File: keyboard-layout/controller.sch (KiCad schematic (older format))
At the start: 15 parts, among them J1 USB_mini_micro_B, SW1 SW_PUSH, X1 XTAL_GND

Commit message: mx footprints
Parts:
- removed C1, C2: 22p, Capacitors_SMD:C_0805_HandSoldering, symbol C
- removed C3, C4, C5: 0.1u, Capacitors_SMD:C_0805_HandSoldering, symbol C
- removed C6: 4.7u, Capacitors_SMD:C_0805_HandSoldering, symbol C
- removed C7: 1u, Capacitors_SMD:C_0805_HandSoldering, symbol C
- removed J1: USB_mini_micro_B, keyboard_parts:USB_miniB_hirose_5S8, symbol USB_mini_micro_B
- removed MCU1: AT90USB1286, AT90USB1286-AU:QFP80P1600X1600X120-64N, symbol AT90USB1286
- removed R1, R2: 10k, Resistors_SMD:R_0805_HandSoldering, symbol R
- removed R3, R4: 22, Resistors_SMD:R_0805_HandSoldering, symbol R
- removed SW1: SW_PUSH, Buttons_Switches_SMD:SW_SPST_TL3342, symbol SW_PUSH
- removed X1: XTAL_GND, Crystals:Crystal_SMD_SeikoEpson_FA238-4pin_3.2x2.5mm, symbol XTAL_GND
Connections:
- no-connect marks 45 -> 0
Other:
- note removed: "HWB (Bootloader)"

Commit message: pcb progress
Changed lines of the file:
@@
 $EndDescr
 $Sheet
-S 8100 2050 2100 1650
+S 5000 1400 1400 3000
 U 5AFAEA09
 F0 "Keyboard Matrix" 60
 F1 "Matrix.sch" 60
-F2 "col0" I L 8100 3000 60
-F3 "col1" I L 8100 3150 60
-F4 "row0" I L 8100 2700 60
-F5 "row1" I L 8100 2850 60
+F2 "row0" I L 5000 1500 60
+F3 "row1" I L 5000 1600 60
+F4 "col0" I L 5000 2100 60
+F5 "row2" I L 5000 1700 60
+F6 "row3" I L 5000 1800 60
+F7 "row4" I L 5000 1900 60
+F8 "row5" I L 5000 2000 60
+F9 "col1" I L 5000 2200 60
+F10 "col2" I L 5000 2300 60
+F11 "col3" I L 5000 2400 60
+F12 "col4" I L 5000 2500 60
+F13 "col5" I L 5000 2600 60
+F14 "col6" I L 5000 2700 60
+F15 "col7" I L 5000 2800 60
+F16 "col8" I L 5000 2900 60
+F17 "col9" I L 5000 3000 60
+F18 "col10" I L 5000 3100 60
+F19 "col11" I L 5000 3200 60
+F20 "col12" I L 5000 3300 60
+F21 "col13" I L 5000 3400 60
+F22 "col14" I L 5000 3500 60
+F23 "col15" I L 5000 3600 60
+F24 "col16" I L 5000 3700 60
+F25 "col17" I L 5000 3800 60
+F26 "col18" I L 5000 3900 60
+F27 "col19" I L 5000 4000 60
+F28 "col20" I L 5000 4100 60
 $EndSheet
+Wire Wire Line
+	3250 1500 5000 1500
+Wire Wire Line
+	5000 1600 3250 1600
 $Sheet
-S 4950 2050 1400 1650
+S 1850 1400 1400 3000
 U 5B003DFC
 F0 "MCU" 60
 F1 "MCU.sch" 60
-F2 "row0" I R 6350 2700 60
-F3 "row1" I R 6350 2850 60
-F4 "col0" I R 6350 3000 60
-F5 "col1" I R 6350 3150 60
+F2 "row0" I R 3250 1500 60
+F3 "row1" I R 3250 1600 60
+F4 "row2" I R 3250 1700 60
+F5 "row3" I R 3250 1800 60
+F6 "row4" I R 3250 1900 60
+F7 "row5" I R 3250 2000 60
+F8 "col0" I R 3250 2100 60
+F9 "col1" I R 3250 2200 60
+F10 "col2" I R 3250 2300 60
+F11 "col3" I R 3250 2400 60
+F12 "col4" I R 3250 2500 60
+F13 "col5" I R 3250 2600 60
+F14 "col6" I R 3250 2700 60
+F15 "col7" I R 3250 2800 60
+F16 "col8" I R 3250 2900 60
+F17 "col9" I R 3250 3000 60
+F18 "col10" I R 3250 3100 60
+F19 "col11" I R 3250 3200 60
+F20 "col12" I R 3250 3300 60
+F21 "col13" I R 3250 3400 60
+F22 "col14" I R 3250 3500 60
+F23 "col15" I R 3250 3600 60
+F24 "col16" I R 3250 3700 60
+F25 "col17" I R 3250 3800 60
+F26 "col18" I R 3250 3900 60
+F27 "col19" I R 3250 4000 60
+F28 "col20" I R 3250 4100 60
 $EndSheet
 Wire Wire Line
-	6350 2700 8100 2700
+	3250 1700 5000 1700
 Wire Wire Line
-	6350 2850 8100 2850
+	5000 1700 5000 1800
 Wire Wire Line
-	6350 3000 8100 3000
+	5000 1800 3250 1800
 Wire Wire Line
-	8100 3150 6350 3150
+	3250 1900 5000 1900
+Wire Wire Line
+	5000 2000 3250 2000
+Wire Wire Line
+	3250 2100 5000 2100
+Wire Wire Line
+	5000 2200 3250 2200
+Wire Wire Line
+	3250 2300 5000 2300
+Wire Wire Line
+	5000 2400 3250 2400
+Wire Wire Line
+	3250 2500 5000 2500
+Wire Wire Line
+	5000 2600 3250 2600
+Wire Wire Line
+	3250 2700 5000 2700
+Wire Wire Line
+	5000 2800 3250 2800
+Wire Wire Line
+	3250 2900 5000 2900
+Wire Wire Line
+	5000 3000 3250 3000
+Wire Wire Line
+	3250 3100 5000 3100
+Wire Wire Line
+	5000 3200 3250 3200
+Wire Wire Line
+	3250 3300 5000 3300
+Wire Wire Line
+	5000 3400 3250 3400
+Wire Wire Line
+	3250 3500 5000 3500
+Wire Wire Line
+	5000 3600 3250 3600
+Wire Wire Line
+	3250 3700 5000 3700
+Wire Wire Line
+	5000 3800 3250 3800
+Wire Wire Line
+	3250 3900 5000 3900
+Wire Wire Line
+	5000 4000 3250 4000
+Wire Wire Line
+	3250 4100 5000 4100
 $EndSCHEMATC

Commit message: python scripting
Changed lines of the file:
@@
 F6 "row3" I L 5000 1800 60
 F7 "row4" I L 5000 1900 60
-F8 "row5" I L 5000 2000 60
-F9 "col1" I L 5000 2200 60
-F10 "col2" I L 5000 2300 60
-F11 "col3" I L 5000 2400 60
-F12 "col4" I L 5000 2500 60
-F13 "col5" I L 5000 2600 60
-F14 "col6" I L 5000 2700 60
-F15 "col7" I L 5000 2800 60
-F16 "col8" I L 5000 2900 60
-F17 "col9" I L 5000 3000 60
-F18 "col10" I L 5000 3100 60
-F19 "col11" I L 5000 3200 60
-F20 "col12" I L 5000 3300 60
-F21 "col13" I L 5000 3400 60
-F22 "col14" I L 5000 3500 60
-F23 "col15" I L 5000 3600 60
-F24 "col16" I L 5000 3700 60
-F25 "col17" I L 5000 3800 60
-F26 "col18" I L 5000 3900 60
-F27 "col19" I L 5000 4000 60
-F28 "col20" I L 5000 4100 60
+F8 "col1" I L 5000 2200 60
+F9 "col2" I L 5000 2300 60
+F10 "col3" I L 5000 2400 60
+F11 "col4" I L 5000 2500 60
+F12 "col5" I L 5000 2600 60
+F13 "col6" I L 5000 2700 60
+F14 "col7" I L 5000 2800 60
+F15 "col8" I L 5000 2900 60
+F16 "col9" I L 5000 3000 60
+F17 "col10" I L 5000 3100 60
+F18 "col11" I L 5000 3200 60
+F19 "col12" I L 5000 3300 60
+F20 "col13" I L 5000 3400 60
+F21 "col14" I L 5000 3500 60
+F22 "col15" I L 5000 3600 60
+F23 "col16" I L 5000 3700 60
+F24 "col17" I L 5000 3800 60
+F25 "col18" I L 5000 3900 60
+F26 "col19" I L 5000 4000 60
+F27 "col20" I L 5000 4100 60
 $EndSheet
 Wire Wire Line
@@
 F5 "row3" I R 3250 1800 60
 F6 "row4" I R 3250 1900 60
-F7 "row5" I R 3250 2000 60
-F8 "col0" I R 3250 2100 60
-F9 "col1" I R 3250 2200 60
-F10 "col2" I R 3250 2300 60
-F11 "col3" I R 3250 2400 60
-F12 "col4" I R 3250 2500 60
-F13 "col5" I R 3250 2600 60
-F14 "col6" I R 3250 2700 60
-F15 "col7" I R 3250 2800 60
-F16 "col8" I R 3250 2900 60
-F17 "col9" I R 3250 3000 60
-F18 "col10" I R 3250 3100 60
-F19 "col11" I R 3250 3200 60
-F20 "col12" I R 3250 3300 60
-F21 "col13" I R 3250 3400 60
-F22 "col14" I R 3250 3500 60
-F23 "col15" I R 3250 3600 60
-F24 "col16" I R 3250 3700 60
-F25 "col17" I R 3250 3800 60
-F26 "col18" I R 3250 3900 60
-F27 "col19" I R 3250 4000 60
-F28 "col20" I R 3250 4100 60
+F7 "col0" I R 3250 2100 60
+F8 "col1" I R 3250 2200 60
+F9 "col2" I R 3250 2300 60
+F10 "col3" I R 3250 2400 60
+F11 "col4" I R 3250 2500 60
+F12 "col5" I R 3250 2600 60
+F13 "col6" I R 3250 2700 60
+F14 "col7" I R 3250 2800 60
+F15 "col8" I R 3250 2900 60
+F16 "col9" I R 3250 3000 60
+F17 "col10" I R 3250 3100 60
+F18 "col11" I R 3250 3200 60
+F19 "col12" I R 3250 3300 60
+F20 "col13" I R 3250 3400 60
+F21 "col14" I R 3250 3500 60
+F22 "col15" I R 3250 3600 60
+F23 "col16" I R 3250 3700 60
+F24 "col17" I R 3250 3800 60
+F25 "col18" I R 3250 3900 60
+F26 "col19" I R 3250 4000 60
+F27 "col20" I R 3250 4100 60
 $EndSheet
 Wire Wire Line
@@
 	3250 1900 5000 1900
 Wire Wire Line
-	5000 2000 3250 2000
-Wire Wire Line
 	3250 2100 5000 2100

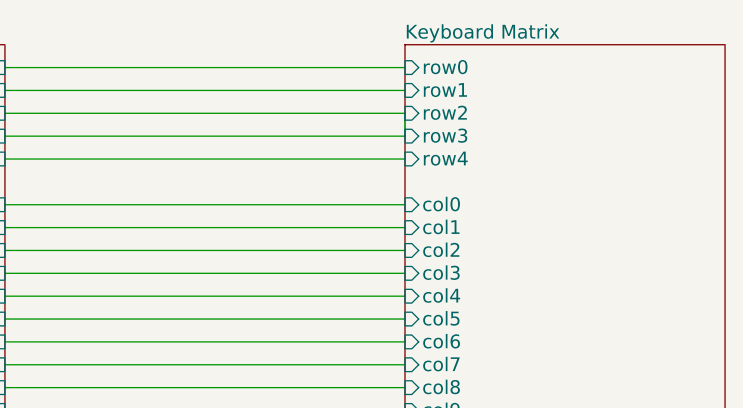
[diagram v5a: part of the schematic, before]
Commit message: pcb without leds finished
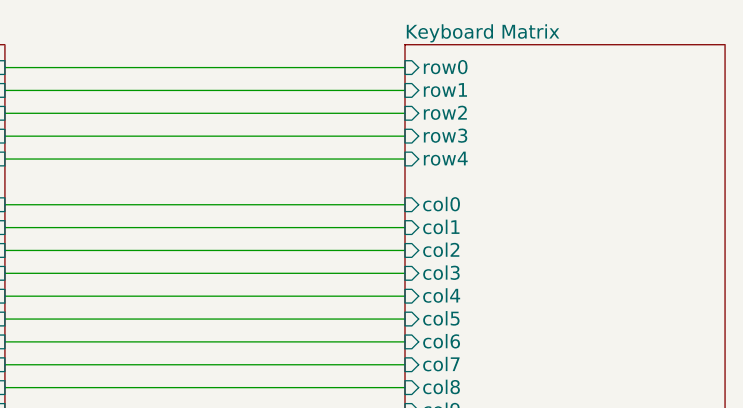
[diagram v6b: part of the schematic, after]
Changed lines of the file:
@@
 Comment4 ""
 $EndDescr
-$Sheet
-S 5000 1400 1400 3000
-U 5AFAEA09
-F0 "Keyboard Matrix" 60
-F1 "Matrix.sch" 60
-F2 "row0" I L 5000 1500 60
-F3 "row1" I L 5000 1600 60
-F4 "col0" I L 5000 2100 60
-F5 "row2" I L 5000 1700 60
-F6 "row3" I L 5000 1800 60
-F7 "row4" I L 5000 1900 60
-F8 "col1" I L 5000 2200 60
-F9 "col2" I L 5000 2300 60
-F10 "col3" I L 5000 2400 60
-F11 "col4" I L 5000 2500 60
-F12 "col5" I L 5000 2600 60
-F13 "col6" I L 5000 2700 60
-F14 "col7" I L 5000 2800 60
-F15 "col8" I L 5000 2900 60
-F16 "col9" I L 5000 3000 60
-F17 "col10" I L 5000 3100 60
-F18 "col11" I L 5000 3200 60
-F19 "col12" I L 5000 3300 60
-F20 "col13" I L 5000 3400 60
-F21 "col14" I L 5000 3500 60
-F22 "col15" I L 5000 3600 60
-F23 "col16" I L 5000 3700 60
-F24 "col17" I L 5000 3800 60
-F25 "col18" I L 5000 3900 60
-F26 "col19" I L 5000 4000 60
-F27 "col20" I L 5000 4100 60
-$EndSheet
 Wire Wire Line
 	3250 1500 5000 1500
@@
 F27 "col20" I R 3250 4100 60
 $EndSheet
-Wire Wire Line
-	3250 1700 5000 1700
-Wire Wire Line
-	5000 1700 5000 1800
-Wire Wire Line
-	5000 1800 3250 1800
-Wire Wire Line
-	3250 1900 5000 1900
 Wire Wire Line
 	3250 2100 5000 2100
@@
 Wire Wire Line
 	3250 4100 5000 4100
+$Sheet
+S 5000 1400 1400 3000
+U 5AFAEA09
+F0 "Keyboard Matrix" 60
+F1 "Matrix.sch" 60
+F2 "row0" I L 5000 1500 60
+F3 "row1" I L 5000 1600 60
+F4 "col0" I L 5000 2100 60
+F5 "row2" I L 5000 1700 60
+F6 "row3" I L 5000 1800 60
+F7 "row4" I L 5000 1900 60
+F8 "col1" I L 5000 2200 60
+F9 "col2" I L 5000 2300 60
+F10 "col3" I L 5000 2400 60
+F11 "col4" I L 5000 2500 60
+F12 "col5" I L 5000 2600 60
+F13 "col6" I L 5000 2700 60
+F14 "col7" I L 5000 2800 60
+F15 "col8" I L 5000 2900 60
+F16 "col9" I L 5000 3000 60
+F17 "col10" I L 5000 3100 60
+F18 "col11" I L 5000 3200 60
+F19 "col12" I L 5000 3300 60
+F20 "col13" I L 5000 3400 60
+F21 "col14" I L 5000 3500 60
+F22 "col15" I L 5000 3600 60
+F23 "col16" I L 5000 3700 60
+F24 "col17" I L 5000 3800 60
+F25 "col18" I L 5000 3900 60
+F26 "col19" I L 5000 4000 60
+F27 "col20" I L 5000 4100 60
+$EndSheet
+Wire Wire Line
+	3250 1900 5000 1900
+Wire Wire Line
+	5000 1800 3250 1800
+Wire Wire Line
+	3250 1700 5000 1700
 $EndSCHEMATC

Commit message: Leds
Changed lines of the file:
@@
 $Descr A4 11693 8268
 encoding utf-8
-Sheet 1 3
+Sheet 1 4
 Title ""
 Date ""
@@
 $EndDescr
 Wire Wire Line
-	3250 1500 5000 1500
+	5600 1650 7350 1650
 Wire Wire Line
-	5000 1600 3250 1600
+	7350 1750 5600 1750
 $Sheet
-S 1850 1400 1400 3000
+S 4200 1550 1400 3000
 U 5B003DFC
 F0 "MCU" 60
 F1 "MCU.sch" 60
-F2 "row0" I R 3250 1500 60
-F3 "row1" I R 3250 1600 60
-F4 "row2" I R 3250 1700 60
-F5 "row3" I R 3250 1800 60
-F6 "row4" I R 3250 1900 60
-F7 "col0" I R 3250 2100 60
-F8 "col1" I R 3250 2200 60
-F9 "col2" I R 3250 2300 60
-F10 "col3" I R 3250 2400 60
-F11 "col4" I R 3250 2500 60
-F12 "col5" I R 3250 2600 60
-F13 "col6" I R 3250 2700 60
-F14 "col7" I R 3250 2800 60
-F15 "col8" I R 3250 2900 60
-F16 "col9" I R 3250 3000 60
-F17 "col10" I R 3250 3100 60
-F18 "col11" I R 3250 3200 60
-F19 "col12" I R 3250 3300 60
-F20 "col13" I R 3250 3400 60
-F21 "col14" I R 3250 3500 60
-F22 "col15" I R 3250 3600 60
-F23 "col16" I R 3250 3700 60
-F24 "col17" I R 3250 3800 60
-F25 "col18" I R 3250 3900 60
-F26 "col19" I R 3250 4000 60
-F27 "col20" I R 3250 4100 60
+F2 "row0" I R 5600 1650 60
+F3 "row1" I R 5600 1750 60
+F4 "row2" I R 5600 1850 60
+F5 "row3" I R 5600 1950 60
+F6 "row4" I R 5600 2050 60
+F7 "col0" I R 5600 2250 60
+F8 "col1" I R 5600 2350 60
+F9 "col2" I R 5600 2450 60
+F10 "col3" I R 5600 2550 60
+F11 "col4" I R 5600 2650 60
+F12 "col5" I R 5600 2750 60
+F13 "col6" I R 5600 2850 60
+F14 "col7" I R 5600 2950 60
+F15 "col8" I R 5600 3050 60
+F16 "col9" I R 5600 3150 60
+F17 "col10" I R 5600 3250 60
+F18 "col11" I R 5600 3350 60
+F19 "col12" I R 5600 3450 60
+F20 "col13" I R 5600 3550 60
+F21 "col14" I R 5600 3650 60
+F22 "col15" I R 5600 3750 60
+F23 "col16" I R 5600 3850 60
+F24 "col17" I R 5600 3950 60
+F25 "col18" I R 5600 4050 60
+F26 "col19" I R 5600 4150 60
+F27 "col20" I R 5600 4250 60
+F28 "Mosfet" I L 4200 2150 60
 $EndSheet
 Wire Wire Line
-	3250 2100 5000 2100
+	5600 2250 7350 2250
 Wire Wire Line
-	5000 2200 3250 2200
+	7350 2350 5600 2350
 Wire Wire Line
-	3250 2300 5000 2300
+	5600 2450 7350 2450
 Wire Wire Line
-	5000 2400 3250 2400
+	7350 2550 5600 2550
 Wire Wire Line
-	3250 2500 5000 2500
+	5600 2650 7350 2650
 Wire Wire Line
-	5000 2600 3250 2600
+	7350 2750 5600 2750
 Wire Wire Line
-	3250 2700 5000 2700
+	5600 2850 7350 2850
 Wire Wire Line
-	5000 2800 3250 2800
+	7350 2950 5600 2950
 Wire Wire Line
-	3250 2900 5000 2900
+	5600 3050 7350 3050
 Wire Wire Line
-	5000 3000 3250 3000
+	7350 3150 5600 3150
 Wire Wire Line
-	3250 3100 5000 3100
+	5600 3250 7350 3250
 Wire Wire Line
-	5000 3200 3250 3200
+	7350 3350 5600 3350
 Wire Wire Line
-	3250 3300 5000 3300
+	5600 3450 7350 3450
 Wire Wire Line
-	5000 3400 3250 3400
+	7350 3550 5600 3550
 Wire Wire Line
-	3250 3500 5000 3500
+	5600 3650 7350 3650
 Wire Wire Line
-	5000 3600 3250 3600
+	7350 3750 5600 3750
 Wire Wire Line
-	3250 3700 5000 3700
+	5600 3850 7350 3850
 Wire Wire Line
-	5000 3800 3250 3800
+	7350 3950 5600 3950
 Wire Wire Line
-	3250 3900 5000 3900
+	5600 4050 7350 4050
 Wire Wire Line
-	5000 4000 3250 4000
+	7350 4150 5600 4150
 Wire Wire Line
-	3250 4100 5000 4100
+	5600 4250 7350 4250
 $Sheet
-S 5000 1400 1400 3000
+S 7350 1550 1400 3000
 U 5AFAEA09
 F0 "Keyboard Matrix" 60
 F1 "Matrix.sch" 60
-F2 "row0" I L 5000 1500 60
-F3 "row1" I L 5000 1600 60
-F4 "col0" I L 5000 2100 60
-F5 "row2" I L 5000 1700 60
-F6 "row3" I L 5000 1800 60
-F7 "row4" I L 5000 1900 60
-F8 "col1" I L 5000 2200 60
-F9 "col2" I L 5000 2300 60
-F10 "col3" I L 5000 2400 60
-F11 "col4" I L 5000 2500 60
-F12 "col5" I L 5000 2600 60
-F13 "col6" I L 5000 2700 60
-F14 "col7" I L 5000 2800 60
-F15 "col8" I L 5000 2900 60
-F16 "col9" I L 5000 3000 60
-F17 "col10" I L 5000 3100 60
-F18 "col11" I L 5000 3200 60
-F19 "col12" I L 5000 3300 60
-F20 "col13" I L 5000 3400 60
-F21 "col14" I L 5000 3500 60
-F22 "col15" I L 5000 3600 60
-F23 "col16" I L 5000 3700 60
-F24 "col17" I L 5000 3800 60
-F25 "col18" I L 5000 3900 60
-F26 "col19" I L 5000 4000 60
-F27 "col20" I L 5000 4100 60
+F2 "row0" I L 7350 1650 60
+F3 "row1" I L 7350 1750 60
+F4 "col0" I L 7350 2250 60
+F5 "row2" I L 7350 1850 60
+F6 "row3" I L 7350 1950 60
+F7 "row4" I L 7350 2050 60
+F8 "col1" I L 7350 2350 60
+F9 "col2" I L 7350 2450 60
+F10 "col3" I L 7350 2550 60
+F11 "col4" I L 7350 2650 60
+F12 "col5" I L 7350 2750 60
+F13 "col6" I L 7350 2850 60
+F14 "col7" I L 7350 2950 60
+F15 "col8" I L 7350 3050 60
+F16 "col9" I L 7350 3150 60
+F17 "col10" I L 7350 3250 60
+F18 "col11" I L 7350 3350 60
+F19 "col12" I L 7350 3450 60
+F20 "col13" I L 7350 3550 60
+F21 "col14" I L 7350 3650 60
+F22 "col15" I L 7350 3750 60
+F23 "col16" I L 7350 3850 60
+F24 "col17" I L 7350 3950 60
+F25 "col18" I L 7350 4050 60
+F26 "col19" I L 7350 4150 60
+F27 "col20" I L 7350 4250 60
 $EndSheet
 Wire Wire Line
-	3250 1900 5000 1900
+	5600 2050 7350 2050
 Wire Wire Line
-	5000 1800 3250 1800
+	7350 1950 5600 1950
 Wire Wire Line
-	3250 1700 5000 1700
+	5600 1850 7350 1850
+$Sheet
+S 1550 1900 1700 1550
+U 5B204446
+F0 "leds" 60
+F1 "leds.sch" 60
+F2 "Mosfet" I R 3250 2150 60
+$EndSheet
+Wire Wire Line
+	3250 2150 4200 2150
 $EndSCHEMATC
